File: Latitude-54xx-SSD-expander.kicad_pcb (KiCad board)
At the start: 4 copper layers, 60 x 112 mm, 35 parts, among them J1 Bus_M.2_Socket_M, J2 Bus_M.2_Socket_M, J3 Bus_M.2_Socket_M, J4 qwiic, U1 clockbuffer_9ZXL0651AKLF

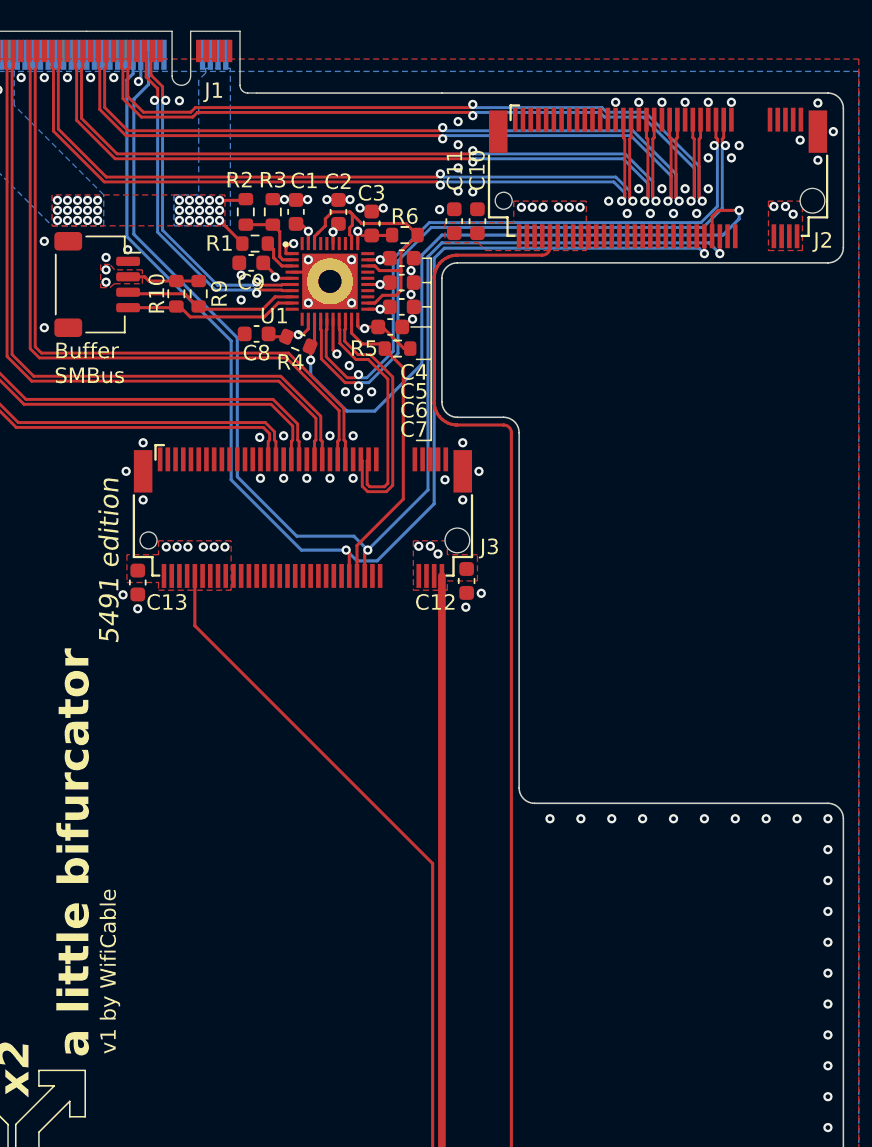
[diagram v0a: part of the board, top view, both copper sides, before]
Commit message: Connected PEDET for first slot
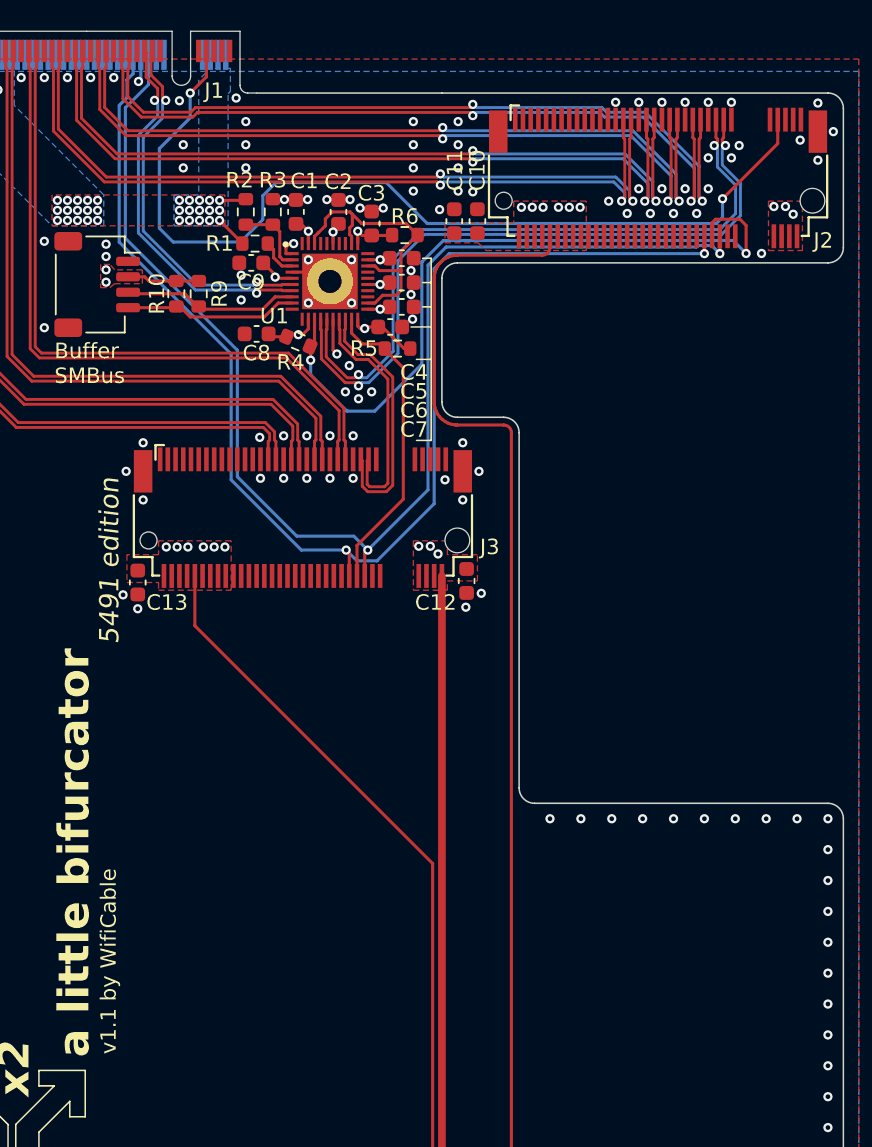
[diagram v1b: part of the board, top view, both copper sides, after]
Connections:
- J1 pad 69: unconnected-(J1-PEDET-Pad69) -> Net-(J1-PEDET)
- J2 pad 69: unconnected-(J2-PEDET-Pad69) -> Net-(J1-PEDET)
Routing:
- net Net-(J1-PEDET): track 0.00 -> 61.2 mm, vias 0 -> 2
- net SSD1_REFCLK-: track 42.5 -> 44.4 mm
- net SSD1_REFCLK+: track 43.5 -> 45.4 mm
- net Host_REFCLK-: track 22.7 -> 24.5 mm
- net Host_REFCLK+: track 22.2 -> 24.0 mm
- net SSD1_CLKREQ#: track 45.5 -> 46.8 mm
- net GND: vias 202 -> 213
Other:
- board text added: "TODO: [x] Properly look into the mounting method to the chassis -[ ] Cut off unused PCB area near the end [x] Come up with a better name/logo [x] diffpair ground vias [x] M.2 slot capacitors -[ ] remove ground around diffpairs? [x] more ground vias [x] wire up PEDET for slot 1 (why not lol)"
- board text added: "v1.1 by WifiCable"
- board text removed: "TODO: [x] Properly look into the mounting method to the chassis -[ ] Cut off unused PCB area near the end [x] Come up with a better name/logo [x] diffpair ground vias [x] M.2 slot capacitors -[ ] remove ground around diffpairs? [x] more ground vias"
- board text removed: "v1 by WifiCable"

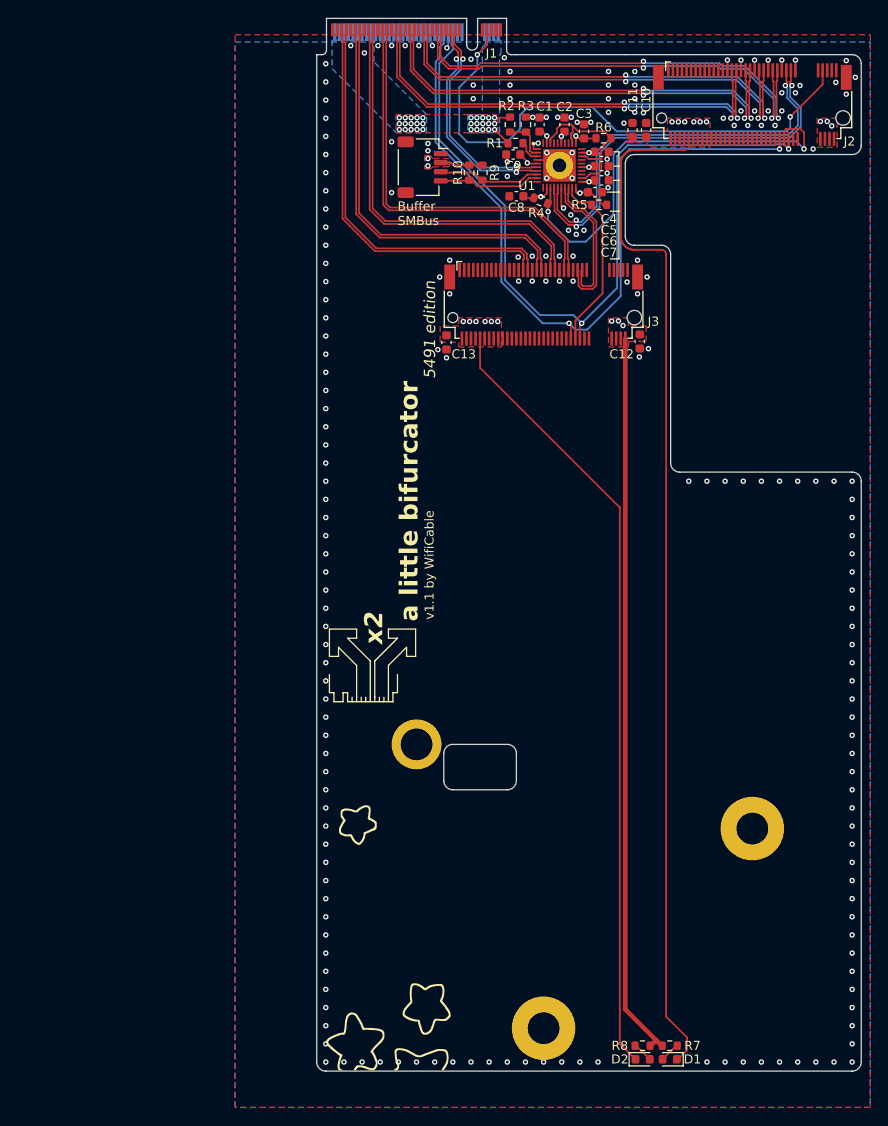
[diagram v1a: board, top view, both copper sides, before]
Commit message: v2
replaced buffer with 9DBL411BGLFT, fixed impedance (for JLC), added spare refclk breakouts, added ssd smbus breakout, added host activity LED option, improved PCIe pair layout. todo: fix standoff footprints
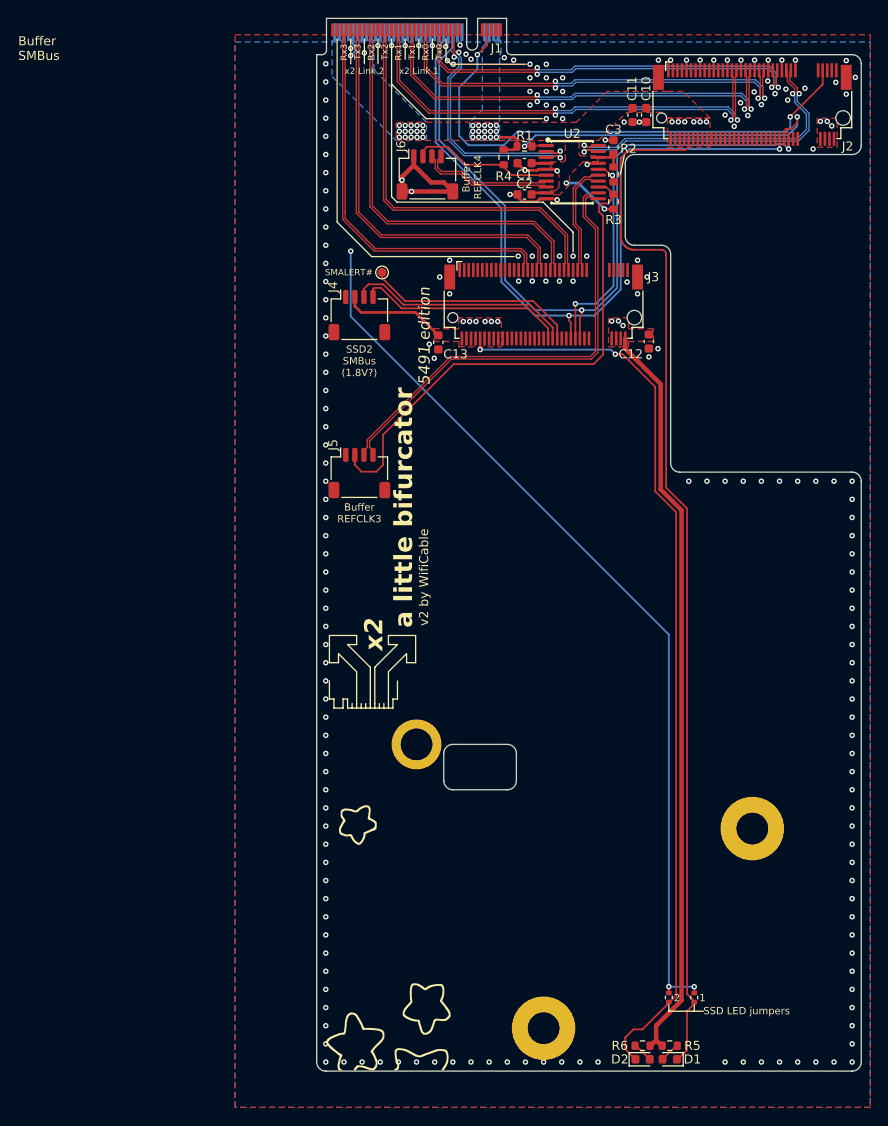
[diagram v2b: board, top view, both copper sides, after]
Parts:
- removed C4, C5, C6, C7, C8, C9: 100nF, Capacitor_SMD:C_0603_1608Metric
- removed H4: MountingHole_Pad, TestPoint:TestPoint_THTPad_D3.0mm_Drill1.5mm
- removed R10, R9: 10kΩ, Resistor_SMD:R_0603_1608Metric
- removed R7, R8: 5K1, Resistor_SMD:R_0603_1608Metric
- removed U1: clockbuffer_9ZXL0651AKLF, A-my-stuff:clockbuffer_9ZXL0651AKLF
- added J5: refqwock, Connector_JST:JST_SH_SM04B-SRSS-TB_1x04-1MP_P1.00mm_Horizontal, F.Cu at (83.7, 90.1)
- added J6: refqwock, Connector_JST:JST_SH_SM04B-SRSS-TB_1x04-1MP_P1.00mm_Horizontal, F.Cu at (91.2, 57.2)
- added JP1: SSD1_ledjumper, Resistor_SMD:R_0402_1005Metric, F.Cu at (120.6, 147.9)
- added JP2: SSD2_ledjumper, Resistor_SMD:R_0402_1005Metric, F.Cu at (117.8, 147.9)
- added TP1: smalert, TestPoint:TestPoint_Pad_D1.0mm, F.Cu at (86.2, 68.0)
- added U2: clockbuffer_RENESAS_9DBL411BGLFT, A-my-stuff:clockbuffer_RENESAS 9DBL411BGLFT, F.Cu at (107.2, 57.0)
- J2, J3: value Bus_M.2_Socket_M -> M-key-full; footprint A_my_stuff:m-key -> A-my-stuff:m-key
- R5, R6: value 10kΩ -> 5K1
- moved R6 100.1 mm to (114.9, 153.2)
- moved R5 93.0 mm to (117.9, 153.2)
- moved J4 17.7 mm to (83.7, 72.7), turned to 0 degrees
- moved R3 12.9 mm to (111.7, 60.2)
- moved R2 12.7 mm to (111.7, 57.2)
- moved C2 8.87 mm to (101.9, 59.4), turned to 180 degrees
- moved R4 6.31 mm to (99.6, 55.3), turned to -90 degrees
- moved C1 4.56 mm to (101.9, 56.0), turned to 180 degrees
- moved C3 3.69 mm to (111.7, 54.2)
- moved C10 1.65 mm to (115.3, 50.6), turned to -90 degrees
- moved C11 1.65 mm to (113.8, 50.6), turned to -90 degrees
- moved R1 1.06 mm to (101.9, 54.1)
- moved C12 1.00 mm to (115.6, 75.6)
- moved C13 0.90 mm to (92.4, 75.7)
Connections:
- net Net-(D1-K) renamed SSD1_LED#
- net Net-(D2-K) renamed SSD2_LED#
- net Net-(J1-PEDET) renamed SSD1_PEDET#
- J1 pad 10: unconnected-(J1-DAS/~{DSS}/~{LED1}-Pad10) -> Net-(J1-DAS/~{DSS}/~{LED1})
- J3 pad 40: unconnected-(J3-NC-Pad40) -> SSD2_SMCLK
- J3 pad 42: unconnected-(J3-NC-Pad42) -> SSD2_SMDAT
- J3 pad 44: unconnected-(J3-NC-Pad44) -> SSD2_SMALERT#
- J4 pad 3: Buffer_SMBus_DAT -> SSD2_SMDAT
- J4 pad 4: Buffer_SMBus_CLK -> SSD2_SMCLK
- R1 pad 2: Net-(U1-CKPWRGD_PD#) -> SSD1_CLKREQ#
- R2 pad 2: Net-(U1-^vHIBW_BYPM_LOBW#) -> SSD2_CLKREQ#
- R3 pad 1: Net-(U1-^vHIBW_BYPM_LOBW#) -> +3.3V
- R3 pad 2: GND -> CLKREQ3#
- R4 pad 2: SSD1_CLKREQ# -> CLKREQ4#
- R5 pad 1: +3.3V -> Net-(D1-A)
- R5 pad 2: SSD2_CLKREQ# -> +3.3V
- R6 pad 1: +3.3V -> Net-(D2-A)
- R6 pad 2: Net-(U1-vOE2#) -> +3.3V
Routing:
- net Net-(J1-DAS/~{DSS}/~{LED1}): track 0.00 -> 124.2 mm, vias 0 -> 4
- net CLKREQ3#: track 0.00 -> 57.0 mm
- net REFCLK3-: track 0.00 -> 50.4 mm
- net REFCLK3+: track 0.00 -> 49.9 mm
- net GND: track 4.49 -> 31.1 mm, vias 213 -> 207
- net SSD2_SMDAT: track 0.00 -> 25.1 mm
- net SSD2_SMALERT#: track 0.00 -> 23.5 mm
- net SSD2_SMCLK: track 0.00 -> 23.2 mm
- net Net-(U1-vOE2#): track 19.5 -> 0.00 mm
- net CLKREQ4#: track 0.00 -> 15.8 mm
- net REFCLK4-: track 0.00 -> 14.6 mm
- net SSD2_LED#: track 86.5 -> 100.6 mm, vias 0 -> 2
- net REFCLK4+: track 0.00 -> 14.1 mm
- net Buffer_SMBus_DAT: track 11.4 -> 0.00 mm
- net Buffer_SMBus_CLK: track 11.2 -> 0.00 mm
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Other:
- board text added: "1"
- board text added: "2"
- board text added: "Buffer REFCLK3"
- board text added: "Buffer REFCLK4"
- board text added: "Rx0"
- board text added: "Rx1"
- board text added: "Rx2"
- board text added: "Rx3"
- board text added: "SMALERT#"
- board text added: "SSD LED jumpers"
- board text added: "SSD2 SMBus (1.8V?)"
- board text added: "Tx0"
- board text added: "Tx1"
- board text added: "Tx2"
- board text added: "Tx3"
- board text added: "v2 TODO: [x] fix impedance (and for jlc now) [x] change clock buffer [ ] use proper m.2 standoffs [x] add host activity led option [x] remove ground around diffpairs"
- board text added: "v2 by WifiCable"
- board text added: "x2 Link 1"
- board text added: "x2 Link 2"
- board text removed: "v1.1 by WifiCable"

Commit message: Minor tweaks
Added pinouts to silkscreen
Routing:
- net GND: vias 207 -> 208
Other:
- board text added: "CLK"
- board text added: "REFCLK pinout: 1:GND 2:CLKREQ# 3:CLK- 4:CLK+"
- board text added: "SMBus pinout: 1:GND 2:3.3V 3:SMDAT 4:SMCLK"
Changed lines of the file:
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@@
 		(tags "capacitor")
 		(property "Reference" "C2"
-			(at 0 1.15 0)
+			(at 2.5 0 0)
 			(layer "F.SilkS")
 			(effects
@@
 	)
 	(gr_line
-		(start 112.9 55.1)
-		(end 112.45 57.25)
+		(start 112.7 55.1)
+		(end 112.7 57.2)
 		(stroke
 			(width 0.1)
@@
 	(gr_line
 		(start 91.75 42.25)
-		(end 91.75 44.5)
+		(end 91.75 45)
 		(stroke
 			(width 0.1)
@@
 	(gr_line
 		(start 90.25 42.25)
-		(end 90.25 44.5)
+		(end 90.25 45)
 		(stroke
 			(width 0.1)
@@
 	(gr_line
 		(start 88.75 42.25)
-		(end 88.75 44.5)
+		(end 88.75 45)
 		(stroke
 			(width 0.1)
@@
 	)
 	(gr_line
+		(start 112.4 57.2)
+		(end 112.7 57.2)
+		(stroke
+			(width 0.1)
+			(type default)
+		)
+		(layer "F.SilkS")
+	)
+	(gr_line
 		(start 84.9 116.000001)
 		(end 84.899999 115.500002)
@@
 		)
 	)
+	(gr_text "CLK"
+		(at 94 42.8 90)
+		(layer "F.SilkS")
+		(effects
+			(font
+				(size 0.7 0.7)
+				(thickness 0.13)
+			)
+			(justify right)
+		)
+	)
 	(gr_text "Buffer\nSMBus"
 		(at 46.1 44.7 0)
@@
 		)
 	)
+	(gr_text "REFCLK pinout:\n1:GND\n2:CLKREQ#\n3:CLK-\n4:CLK+"
+		(at 88.5 87.5 90)
+		(layer "B.SilkS")
+		(effects
+			(font
+				(size 1 1)
+				(thickness 0.15)
+			)
+			(justify left bottom mirror)
+		)
+	)
+	(gr_text "SMBus pinout:\n1:GND\n2:3.3V\n3:SMDAT\n4:SMCLK"
+		(at 88.25 69.75 90)
+		(layer "B.SilkS")
+		(effects
+			(font
+				(size 1 1)
+				(thickness 0.15)
+			)
+			(justify left bottom mirror)
+		)
+	)
 	(gr_text "v2 TODO:\n[x] fix impedance (and for jlc now)\n[x] change clock buffer\n[ ] use proper m.2 standoffs\n[x] add host activity led option\n[x] remove ground around diffpairs"
 		(at 146 62 0)
@@
 	)
 	(via
+		(at 122 155)
+		(size 0.6)
+		(drill 0.3)
+		(layers "F.Cu" "B.Cu")
+		(free yes)
+		(net 82)
+	)
+	(via
 		(at 105.5 60)
 		(size 0.6)
@@
 			(pts
 				(xy 81.1 43.8) (xy 81.8 43.1) (xy 81.8 43.3) (xy 82.4 43.3) (xy 82.4 43.6) (xy 83.1 43.6) (xy 83.1 43.3)
-				(xy 83.9 43.3) (xy 83.9 44.1) (xy 84.6 44.1) (xy 84.6 43.3) (xy 95.5 43.3) (xy 97.2 45) (xy 100.9 45)
-				(xy 101.6 44.3) (xy 116.15 44.3) (xy 116.15 46.5) (xy 134.5 46.5) (xy 134.5 47.3) (xy 131.35 50.45)
-				(xy 131.35 52.3) (xy 122.5 52.35) (xy 122.5 50.9) (xy 119.45 47.85) (xy 116.15 47.85) (xy 110.9 47.85)
-				(xy 107.45 51.3) (xy 87.6 51.3) (xy 87.6 53.6) (xy 104.6 53.6) (xy 104.6 56.4) (xy 105.55 56.4)
-				(xy 105.95 56.8) (xy 105.65 57.1) (xy 105.65 58.05) (xy 104.6 58.75) (xy 104.6 59.7) (xy 105.65 59.7)
-				(xy 106.95 58.4) (xy 106.95 57.3) (xy 108.5 55.75) (xy 110.9 55.75) (xy 110.9 52.8) (xy 111.2 52.5)
-				(xy 111.2 53.8) (xy 112.2 53.8) (xy 112.4 54) (xy 112.4 55.5) (xy 112.4 65.5) (xy 112.1 65.8) (xy 112.1 66.8)
-				(xy 110.9 66.8) (xy 110.9 65.9) (xy 100.85 65.9) (xy 100.85 66.4) (xy 98.9 66.4) (xy 85 66.4) (xy 81.1 62.5)
+				(xy 83.9 43.3) (xy 83.9 44.1) (xy 84.6 44.1) (xy 84.6 43.3) (xy 92.9 43.3) (xy 92.9 43.386) (xy 93.6 43.4)
+				(xy 93.6 43.3) (xy 95.5 43.3) (xy 97.2 45) (xy 100.9 45) (xy 101.6 44.3) (xy 116.15 44.3) (xy 116.15 46.5)
+				(xy 134.5 46.5) (xy 134.5 47.3) (xy 131.35 50.45) (xy 131.35 52.3) (xy 122.5 52.35) (xy 122.5 50.9)
+				(xy 119.45 47.85) (xy 116.15 47.85) (xy 110.9 47.85) (xy 107.45 51.3) (xy 87.6 51.3) (xy 87.6 53.6)
+				(xy 104.6 53.6) (xy 104.6 56.4) (xy 105.55 56.4) (xy 105.95 56.8) (xy 105.65 57.1) (xy 105.65 58.05)
+				(xy 104.6 58.75) (xy 104.6 59.7) (xy 105.65 59.7) (xy 106.95 58.4) (xy 106.95 57.3) (xy 108.5 55.75)
+				(xy 110.9 55.75) (xy 110.9 52.8) (xy 111.2 52.5) (xy 111.2 53.8) (xy 112.2 53.8) (xy 112.4 54) (xy 112.4 55.5)
+				(xy 112.4 65.5) (xy 112.1 65.8) (xy 112.1 66.8) (xy 110.9 66.8) (xy 110.9 65.9) (xy 100.85 65.9)
+				(xy 100.85 66.4) (xy 98.9 66.4) (xy 85 66.4) (xy 81.1 62.5)
 			)
 		)
